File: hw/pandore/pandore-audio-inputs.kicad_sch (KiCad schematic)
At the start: 30 parts, among them J4 XLR+TRS6.35+3SW, J5 XLR+TRS6.35+3SW

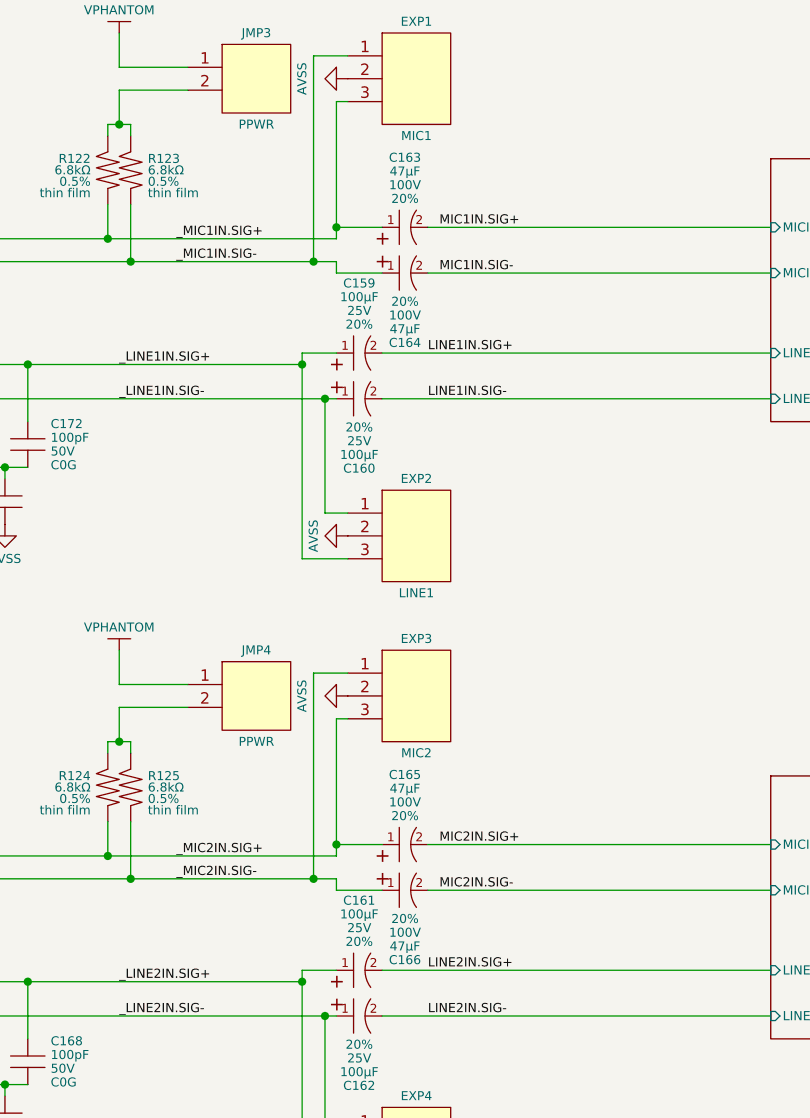
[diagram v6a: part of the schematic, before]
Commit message: finished adding mpn,mfg to all parts, finished routing placement
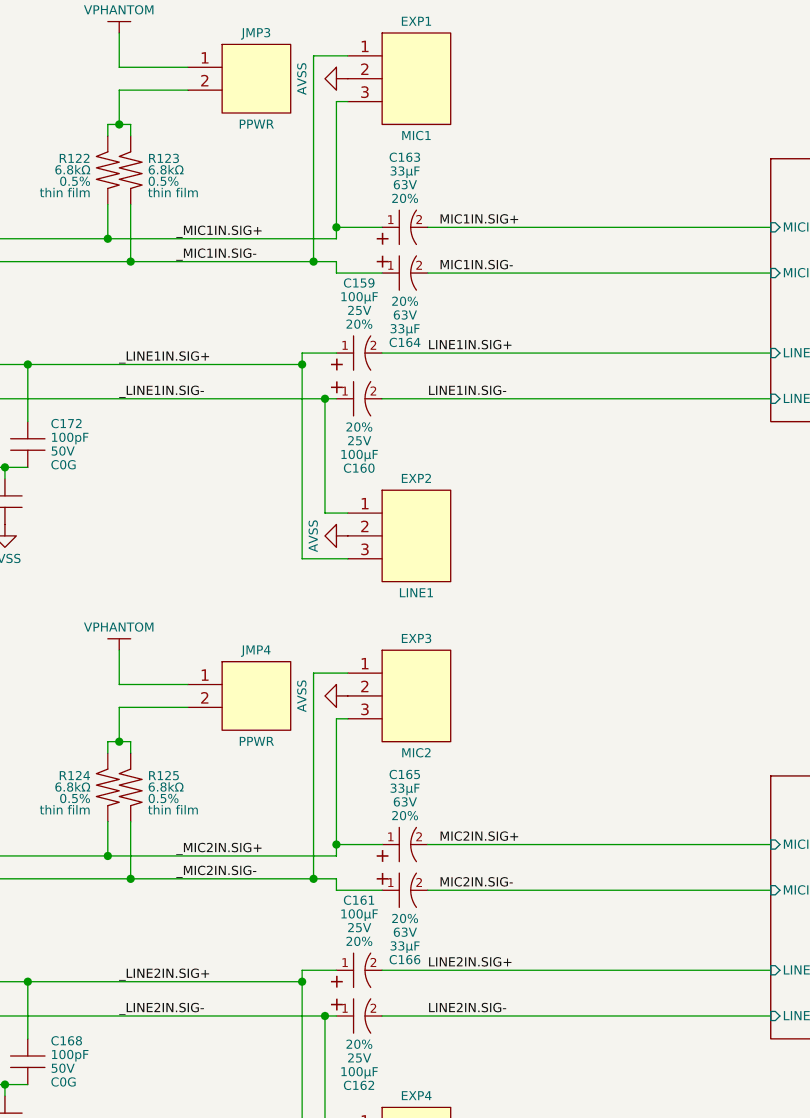
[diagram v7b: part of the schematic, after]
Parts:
- C139, C146, C147, C158, C167, C168, C169, C170, C171, C172: MFG (none) -> Samsung Electro-Mechanics; MPN (none) -> CL10C101JB8NNNC
- C163, C164, C165, C166: Capacitance 47µF -> 33µF; MFG (none) -> KYOCERA AVX; MPN (none) -> APD0609330M063R; Voltage 100V -> 63V
- EXP1, EXP2, EXP3, EXP4: Link url-link -> (none); MFG MFG -> Adam Tech; MPN MPN -> PH1-03-UA
- JMP3, JMP4: Link url-link -> (none); MFG MFG -> Adam Tech; MPN MPN -> PH1-02-UA
- R122, R123, R124, R125: MFG (none) -> Susumu; MPN (none) -> RR1220P-682-D
